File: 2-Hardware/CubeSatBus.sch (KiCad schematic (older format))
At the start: 2 parts

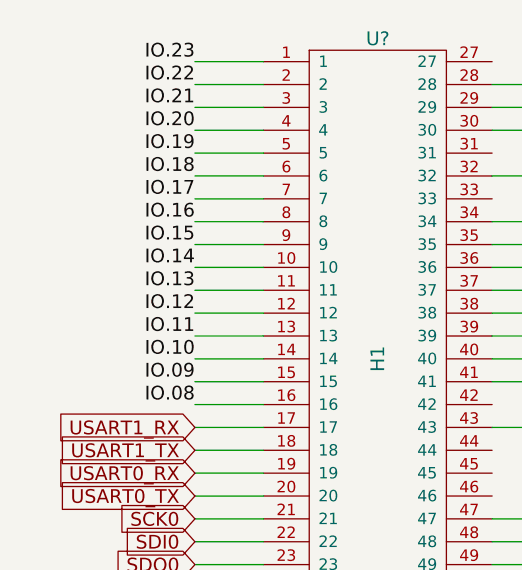
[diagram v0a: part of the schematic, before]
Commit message: Added bus pirate connectors
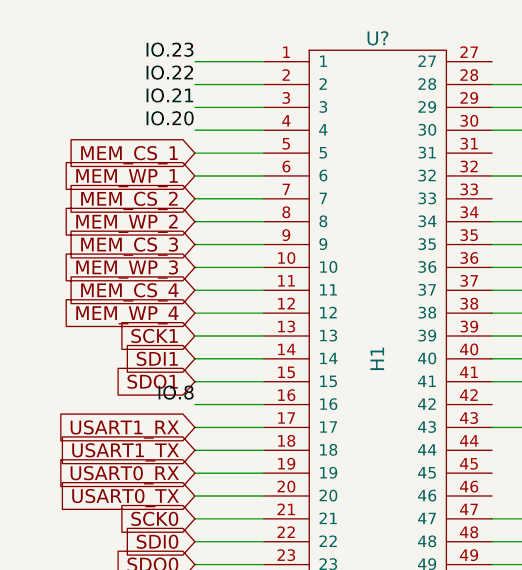
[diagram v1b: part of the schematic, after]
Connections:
- net IO.08 renamed IO.8
- net IO.09 renamed SDO1
- net IO.10 renamed SDI1
- net IO.11 renamed SCK1
- net IO.12 renamed MEM_WP_4
- net IO.13 renamed MEM_CS_4
- net IO.14 renamed MEM_WP_3
- net IO.15 renamed MEM_CS_3
- net IO.16 renamed MEM_WP_2
- net IO.17 renamed MEM_CS_2
- net IO.18 renamed MEM_WP_1
- net IO.19 renamed MEM_CS_1
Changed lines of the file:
@@
 LIBS:TransistorParts
 LIBS:CubeSat
-EELAYER 27 0
+LIBS:BreakoutBoard-cache
+EELAYER 25 0
 EELAYER END
 $Descr A4 11693 8268
 encoding utf-8
-Sheet 2 2
+Sheet 2 3
 Title ""
 Date "7 oct 2014"
@@
 	2750 2400 2500 2400
 $Comp
-L +5V #PWR?
+L +5V #PWR01
 U 1 1 54338DBE
 P 3750 3350
-F 0 "#PWR?" H 3750 3440 20  0001 C CNN
+F 0 "#PWR01" H 3750 3440 20  0001 C CNN
 F 1 "+5V" H 3750 3440 30  0000 C CNN
 F 2 "" H 3750 3350 60  0000 C CNN
@@
 Connection ~ 3750 3400
 $Comp
-L +3.3V #PWR?
+L +3.3V #PWR02
 U 1 1 54338DDF
 P 5500 950
-F 0 "#PWR?" H 5500 910 30  0001 C CNN
+F 0 "#PWR02" H 5500 910 30  0001 C CNN
 F 1 "+3.3V" H 5500 1060 30  0000 C CNN
 F 2 "" H 5500 950 60  0000 C CNN
@@
 Connection ~ 5500 1000
 $Comp
-L GND #PWR?
+L GND #PWR03
 U 1 1 54338E19
 P 5500 1450
-F 0 "#PWR?" H 5500 1450 30  0001 C CNN
+F 0 "#PWR03" H 5500 1450 30  0001 C CNN
 F 1 "GND" H 5500 1380 30  0001 C CNN
 F 2 "" H 5500 1450 60  0000 C CNN
@@
 	5500 1300 5300 1300
 $Comp
-L +BATT #PWR?
+L +BATT #PWR04
 U 1 1 54338E7D
 P 6200 2800
-F 0 "#PWR?" H 6200 2750 20  0001 C CNN
+F 0 "#PWR04" H 6200 2750 20  0001 C CNN
 F 1 "+BATT" H 6200 2900 30  0000 C CNN
 F 2 "" H 6200 2800 60  0000 C CNN
@@
 Text Label 1200 1300 2    60   ~ 0
 IO.20
-Text Label 1200 1400 2    60   ~ 0
-IO.19
-Text Label 1200 1500 2    60   ~ 0
-IO.18
-Text Label 1200 1600 2    60   ~ 0
-IO.17
-Text Label 1200 1700 2    60   ~ 0
-IO.16
-Text Label 1200 1800 2    60   ~ 0
-IO.15
-Text Label 1200 1900 2    60   ~ 0
-IO.14
-Text Label 1200 2000 2    60   ~ 0
-IO.13
-Text Label 1200 2100 2    60   ~ 0
-IO.12
-Text Label 1200 2200 2    60   ~ 0
-IO.11
-Text Label 1200 2300 2    60   ~ 0
-IO.10
-Text Label 1200 2400 2    60   ~ 0
-IO.09
-Text Label 1200 2500 2    60   ~ 0
-IO.08
 Text GLabel 1200 2600 0    60   Input ~ 0
 USART1_RX
@@
 Wire Wire Line
 	2750 1300 2500 1300
+Text GLabel 1200 1400 0    60   Input ~ 0
+MEM_CS_1
+Text GLabel 1200 1500 0    60   Input ~ 0
+MEM_WP_1
+Text GLabel 1200 1600 0    60   Input ~ 0
+MEM_CS_2
+Text GLabel 1200 1700 0    60   Input ~ 0
+MEM_WP_2
+Text GLabel 1200 1800 0    60   Input ~ 0
+MEM_CS_3
+Text GLabel 1200 1900 0    60   Input ~ 0
+MEM_WP_3
+Text GLabel 1200 2000 0    60   Input ~ 0
+MEM_CS_4
+Text GLabel 1200 2100 0    60   Input ~ 0
+MEM_WP_4
+Text GLabel 1200 2200 0    60   Input ~ 0
+SCK1
+Text GLabel 1200 2300 0    60   Input ~ 0
+SDI1
+Text GLabel 1200 2400 0    60   Input ~ 0
+SDO1
+Text Label 1200 2500 2    60   ~ 0
+IO.8
 $EndSCHEMATC
